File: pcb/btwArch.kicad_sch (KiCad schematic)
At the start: 14 parts, among them SW1 SW_Push, SW2 SW_Push, SW3 SW_Push, U1 XIAO-RP2040-SMD

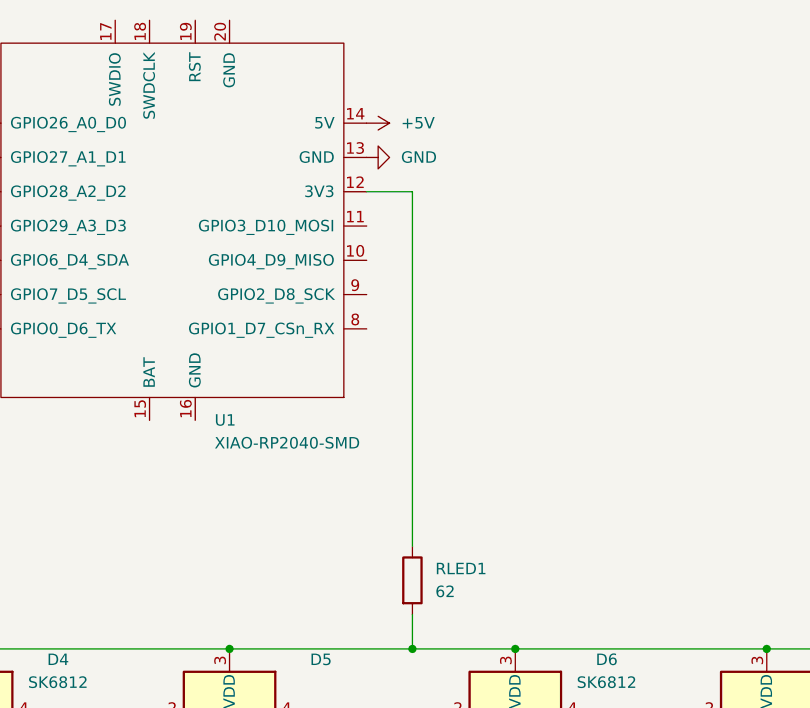
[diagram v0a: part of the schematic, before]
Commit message: Update README and PCB schematic: add banner image and modify power symbol placement
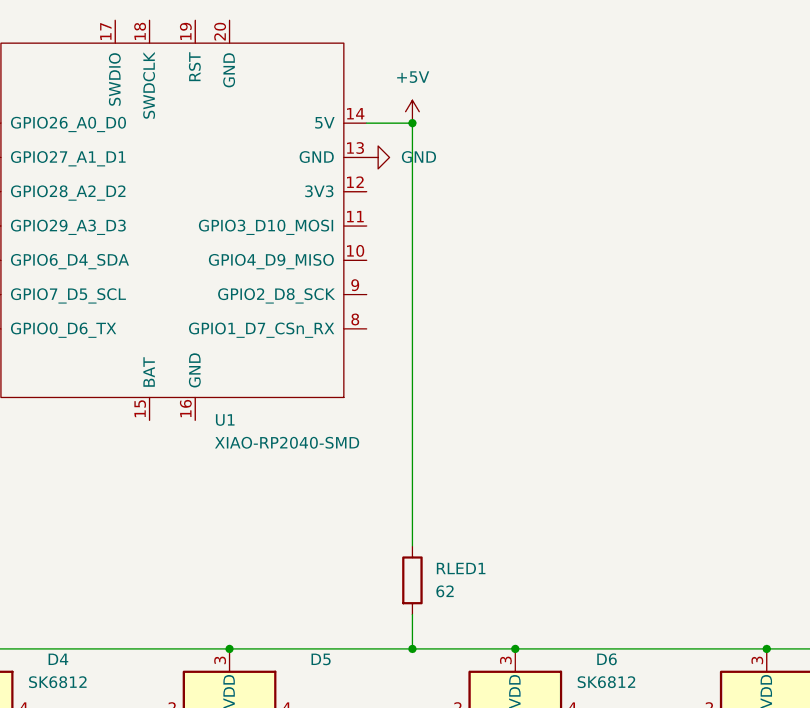
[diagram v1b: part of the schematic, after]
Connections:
- net +5V: now also RLED1.1
- net at U1.12 (3V3): no longer RLED1.1
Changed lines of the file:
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@@
+	)
+	(junction
+		(at 194.31 57.15)
+		(diameter 0)
+		(color 0 0 0 0)
 	)
 	(junction
@@
 	(wire
 		(pts
-			(xy 194.31 64.77) (xy 194.31 104.14)
+			(xy 194.31 57.15) (xy 194.31 104.14)
 		)
 		(stroke
@@
 	(wire
 		(pts
-			(xy 189.23 64.77) (xy 194.31 64.77)
+			(xy 189.23 57.15) (xy 194.31 57.15)
 		)
 		(stroke
@@
 	)
 	(symbol
+		(lib_id "power:+5V")
+		(at 194.31 57.15 0)
+		(unit 1)
+		(exclude_from_sim no)
+		(in_bom yes)
+		(on_board yes)
+		(dnp no)
+		(fields_autoplaced yes)
+		(property "Reference" "#PWR01"
+			(at 194.31 60.96 0)
+			(effects
+				(font
+					(size 1.27 1.27)
+				)
+				(hide yes)
+			)
+		)
+		(property "Value" "+5V"
+			(at 194.31 52.07 0)
+			(effects
+				(font
+					(size 1.27 1.27)
+				)
+			)
+		)
+		(property "Footprint" ""
+			(at 194.31 57.15 0)
+			(effects
+				(font
+					(size 1.27 1.27)
+				)
+				(hide yes)
+			)
+		)
+		(property "Datasheet" ""
+			(at 194.31 57.15 0)
+			(effects
+				(font
+					(size 1.27 1.27)
+				)
+				(hide yes)
+			)
+		)
+		(property "Description" "Power symbol creates a global label with name \"+5V\""
+			(at 194.31 57.15 0)
+			(effects
+				(font
+					(size 1.27 1.27)
+				)
+				(hide yes)
+			)
+		)
+		(pin "1"
+		)
+		(instances
+			(project ""
+				(path "/33dbbadf-34fa-4052-b77b-4250c48f6bb0"
+					(reference "#PWR01")
+					(unit 1)
+				)
+			)
+		)
+	)
+	(symbol
 		(lib_id "LED:SK6812")
 		(at 233.68 123.19 0)
@@
 					(unit 1)
 				)
-			)
-		)
-	)
-	(symbol
-		(lib_id "power:+5V")
-		(at 189.23 57.15 270)
-		(unit 1)
-		(exclude_from_sim no)
-		(in_bom yes)
-		(on_board yes)
-		(dnp no)
-		(fields_autoplaced yes)
-		(property "Reference" "#PWR03"
-			(at 185.42 57.15 0)
-			(effects
-				(font
-					(size 1.27 1.27)
-				)
-				(hide yes)
-			)
-		)
-		(property "Value" "+5V"
-			(at 193.04 57.1499 90)
-			(effects
-				(font
-					(size 1.27 1.27)
-				)
-				(justify left)
-			)
-		)
-		(property "Footprint" ""
-			(at 189.23 57.15 0)
-			(effects
-				(font
-					(size 1.27 1.27)
-				)
-				(hide yes)
-			)
-		)
-		(property "Datasheet" ""
-			(at 189.23 57.15 0)
-			(effects
-				(font
-					(size 1.27 1.27)
-				)
-				(hide yes)
-			)
-		)
-		(property "Description" "Power symbol creates a global label with name \"+5V\""
-			(at 189.23 57.15 0)
-			(effects
-				(font
-					(size 1.27 1.27)
-				)
-				(hide yes)
-			)
-		)
-		(pin "1"
-		)
-		(instances
-			(project ""
-				(path "/33dbbadf-34fa-4052-b77b-4250c48f6bb0"
-					(reference "#PWR03")
-					(unit 1)
-				)
